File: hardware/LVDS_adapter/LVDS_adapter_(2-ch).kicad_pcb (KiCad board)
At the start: 2 copper layers, 26 x 25.8 mm, 10 parts, among them J1 DF12NB(3.0)-30DS-0.5V(51), J2 LVDS, J3 BL_POWER, J4 DF12NB(3.0)-30DS-0.5V(51)

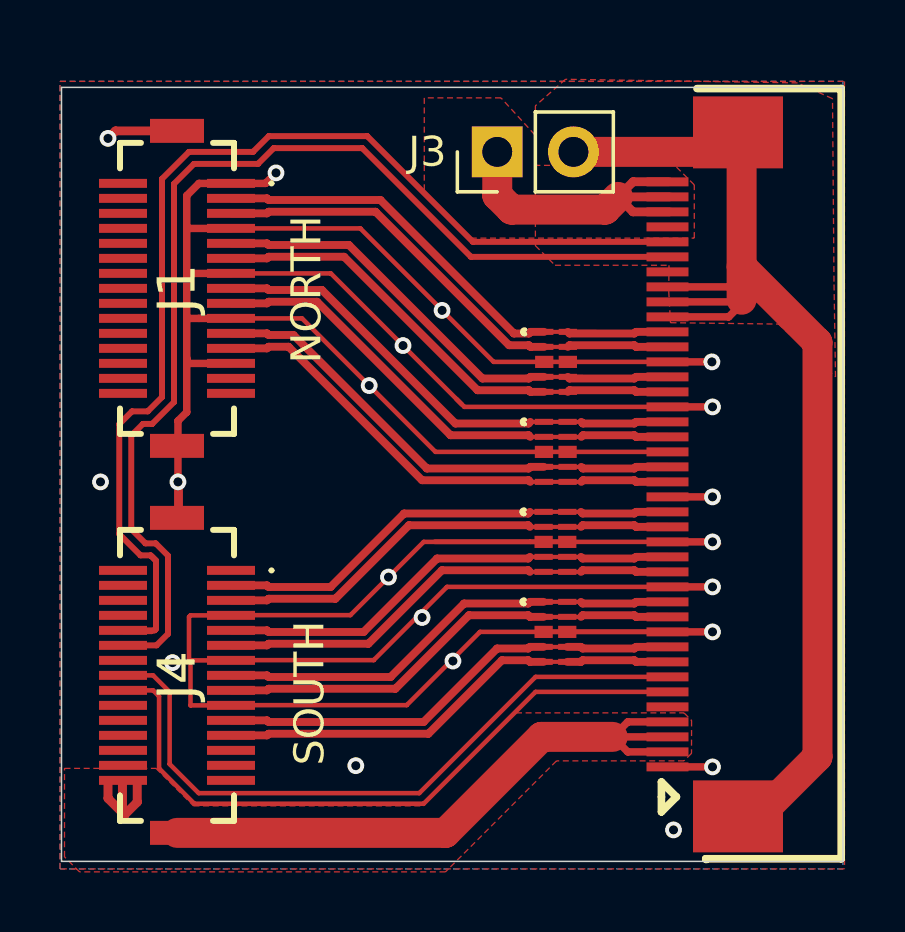
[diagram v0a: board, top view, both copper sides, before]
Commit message: make 4 layers for better signal integrity and add DC-DC for backlight
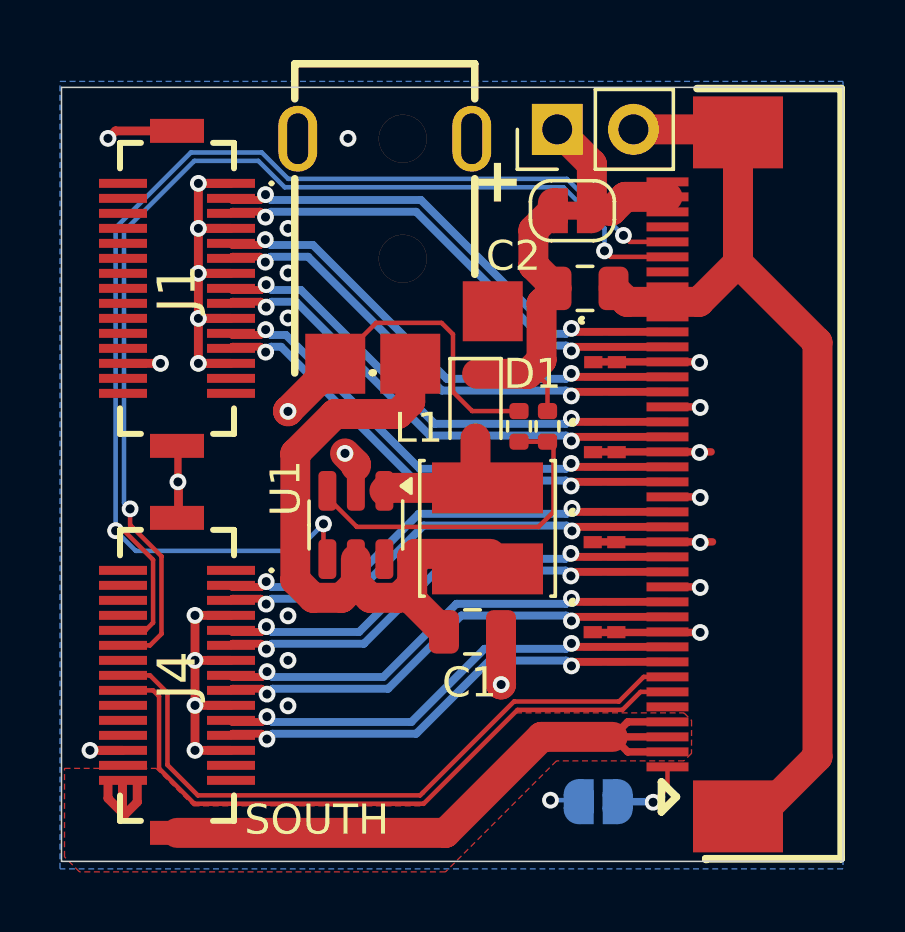
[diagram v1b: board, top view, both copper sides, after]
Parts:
- added C1: 10uF 25V, Capacitor_SMD:C_0805_2012Metric, F.Cu at (138.5, 94.6)
- added C2: 10uF 25V, Capacitor_SMD:C_0805_2012Metric, F.Cu at (142.2, 83.2)
- added D1: 1N5819WS, Diode_SMD:D_SOD-323, F.Cu at (138.6, 87.1)
- added J5: Barrel_Jack_MountingPin, easyeda2kicad:DC-IN-SMD_DC-045A-13A, F.Cu at (135.9, 81.9)
- added JP1: SolderJumper_2_Open, Jumper:SolderJumper-2_P1.3mm_Open_RoundedPad1.0x1.5mm, B.Cu at (142.7, 100.3)
- added JP3: SolderJumper_2_Bridged, Jumper:SolderJumper-2_P1.3mm_Bridged_RoundedPad1.0x1.5mm, F.Cu at (141.8, 80.6)
- added L1: 22uH, Inductor_SMD:L_Cenker_CKCS4020, F.Cu at (139.0, 91.2)
- added R2: 8.06K 1%, Resistor_SMD:R_0402_1005Metric, F.Cu at (140.1, 87.8)
- added R3: 150K 1%, Resistor_SMD:R_0402_1005Metric, F.Cu at (141.0, 87.8)
- added U1: MT3608, Package_TO_SOT_SMD:SOT-23-6, F.Cu at (134.6, 91.0)
- moved G*** 21.3 mm to (128.3, 78.3), turned to 0 degrees
- moved G*** 16.1 mm to (128.7, 92.7), turned to 90 degrees
- moved J3 2.14 mm to (141.3, 77.8)
- moved CR1 1.64 mm to (142.9, 85.6)
- moved CR2 1.64 mm to (142.9, 88.6)
- moved CR3 1.64 mm to (142.9, 91.6)
- moved CR4 1.64 mm to (142.9, 94.6)
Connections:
- CR1 pad 1: LVDS_OC_P -> LVDS_EC_P
- CR1 pad 10: LVDS_OC_P -> LVDS_EC_P
- CR1 pad 2: LVDS_OC_N -> LVDS_EC_N
- CR1 pad 4: LVDS_O2_P -> LVDS_E2_P
- CR1 pad 5: LVDS_O2_N -> LVDS_E2_N
- CR1 pad 6: LVDS_O2_N -> LVDS_E2_N
- CR1 pad 7: LVDS_O2_P -> LVDS_E2_P
- CR1 pad 9: LVDS_OC_N -> LVDS_EC_N
- CR2 pad 1: LVDS_O1_P -> LVDS_E1_P
- CR2 pad 10: LVDS_O1_P -> LVDS_E1_P
- CR2 pad 2: LVDS_O1_N -> LVDS_E1_N
- CR2 pad 4: LVDS_O0_P -> LVDS_E0_P
- CR2 pad 5: LVDS_O0_N -> LVDS_E0_N
- CR2 pad 6: LVDS_O0_N -> LVDS_E0_N
- CR2 pad 7: LVDS_O0_P -> LVDS_E0_P
- CR2 pad 9: LVDS_O1_N -> LVDS_E1_N
- CR3 pad 1: LVDS_EC_P -> LVDS_OC_P
- CR3 pad 10: LVDS_EC_P -> LVDS_OC_P
- CR3 pad 2: LVDS_EC_N -> LVDS_OC_N
- CR3 pad 4: LVDS_E2_P -> LVDS_O2_P
- CR3 pad 5: LVDS_E2_N -> LVDS_O2_N
- CR3 pad 6: LVDS_E2_N -> LVDS_O2_N
- CR3 pad 7: LVDS_E2_P -> LVDS_O2_P
- CR3 pad 9: LVDS_EC_N -> LVDS_OC_N
- CR4 pad 1: LVDS_E1_P -> LVDS_O1_P
- CR4 pad 10: LVDS_E1_P -> LVDS_O1_P
- CR4 pad 2: LVDS_E1_N -> LVDS_O1_N
- CR4 pad 4: LVDS_E0_P -> LVDS_O0_P
- CR4 pad 5: LVDS_E0_N -> LVDS_O0_N
- CR4 pad 6: LVDS_E0_N -> LVDS_O0_N
- CR4 pad 7: LVDS_E0_P -> LVDS_O0_P
- CR4 pad 9: LVDS_E1_N -> LVDS_O1_N
- J1 pad 11: LVDS_O2_N -> LVDS_E2_N
- J1 pad 15: LVDS_O1_P -> LVDS_E1_P
- J1 pad 17: LVDS_O1_N -> LVDS_E1_N
- J1 pad 21: LVDS_O0_P -> LVDS_E0_P
- J1 pad 23: LVDS_O0_N -> LVDS_E0_N
- J1 pad 3: LVDS_OC_P -> LVDS_EC_P
- J1 pad 5: LVDS_OC_N -> LVDS_EC_N
- J1 pad 9: LVDS_O2_P -> LVDS_E2_P
- J2 pad 1: GND -> Net-(J2-Pin_1)
- J2 pad 11: LVDS_E1_N -> LVDS_O1_N
- J2 pad 12: LVDS_E1_P -> LVDS_O1_P
- J2 pad 14: LVDS_E2_N -> LVDS_O2_N
- J2 pad 15: LVDS_E2_P -> LVDS_O2_P
- J2 pad 17: LVDS_EC_N -> LVDS_OC_N
- J2 pad 18: LVDS_EC_P -> LVDS_OC_P
- J2 pad 20: LVDS_O0_N -> LVDS_E0_N
- J2 pad 21: LVDS_O0_P -> LVDS_E0_P
- J2 pad 23: LVDS_O1_N -> LVDS_E1_N
- J2 pad 24: LVDS_O1_P -> LVDS_E1_P
- J2 pad 26: LVDS_O2_N -> LVDS_E2_N
- J2 pad 27: LVDS_O2_P -> LVDS_E2_P
- J2 pad 29: LVDS_OC_N -> LVDS_EC_N
- J2 pad 30: LVDS_OC_P -> LVDS_EC_P
- J2 pad 6: SDA2 -> SCL2
- J2 pad 7: SCL2 -> SDA2
- J2 pad 8: LVDS_E0_N -> LVDS_O0_N
- J2 pad 9: LVDS_E0_P -> LVDS_O0_P
- J4 pad 11: LVDS_E2_N -> LVDS_O2_N
- J4 pad 15: LVDS_E1_P -> LVDS_O1_P
- J4 pad 16: SCL2 -> SDA2
- J4 pad 17: LVDS_E1_N -> LVDS_O1_N
- J4 pad 18: SDA2 -> SCL2
- J4 pad 21: LVDS_E0_P -> LVDS_O0_P
- J4 pad 23: LVDS_E0_N -> LVDS_O0_N
- J4 pad 24: unconnected-(J4-23-Pad24) -> Net-(J4-23)
- J4 pad 3: LVDS_EC_P -> LVDS_OC_P
- J4 pad 5: LVDS_EC_N -> LVDS_OC_N
- J4 pad 9: LVDS_E2_P -> LVDS_O2_P
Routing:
- net GND: track 146.1 -> 47.4 mm, vias 20 -> 28
- net +5V: track 0.00 -> 21.1 mm
- net Net-(U1-FB): track 0.00 -> 11.7 mm
- net Net-(D1-K): track 0.00 -> 11.5 mm
- net LED_GND: track 39.5 -> 46.7 mm, vias 0 -> 3
- net /BL_EN: track 38.0 -> 44.7 mm, vias 0 -> 3
- net LED_VCC: track 11.4 -> 5.90 mm
- net Net-(D1-A): track 0.00 -> 5.29 mm
- net Net-(J2-Pin_1): track 0.00 -> 2.57 mm, vias 0 -> 1
- net LVDS_O2_P: track 17.7 -> 15.9 mm, vias 0 -> 2
- net LVDS_O2_N: track 17.6 -> 15.9 mm, vias 0 -> 2
- net LVDS_OC_N: track 17.5 -> 15.9 mm, vias 0 -> 2
- net LVDS_OC_P: track 17.4 -> 15.9 mm, vias 0 -> 2
- net LVDS_O0_P: track 17.1 -> 15.9 mm, vias 0 -> 2
- net LVDS_EC_N: track 15.7 -> 16.7 mm, vias 0 -> 2
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- added copper zone on In2.Cu, net GND
- added copper zone on In1.Cu, net LED_GND
- removed copper zone on F.Cu, net GND
- removed copper zone on F.Cu, net LED_GND
- removed copper zone on F.Cu, net LED_VCC
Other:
- copper layers 2 -> 4
- board text added: "+"
- board text added: "LVDS adapter v0.11"
- board text added: "VERSION:"
- board text removed: "LVDS adapter board"
- board text removed: "NORTH"
- board text removed: "NOTE: copper fill was corrected (too many short circuits on FPC connector)"

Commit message: review and update manufacturing constraints (via size, etc.)
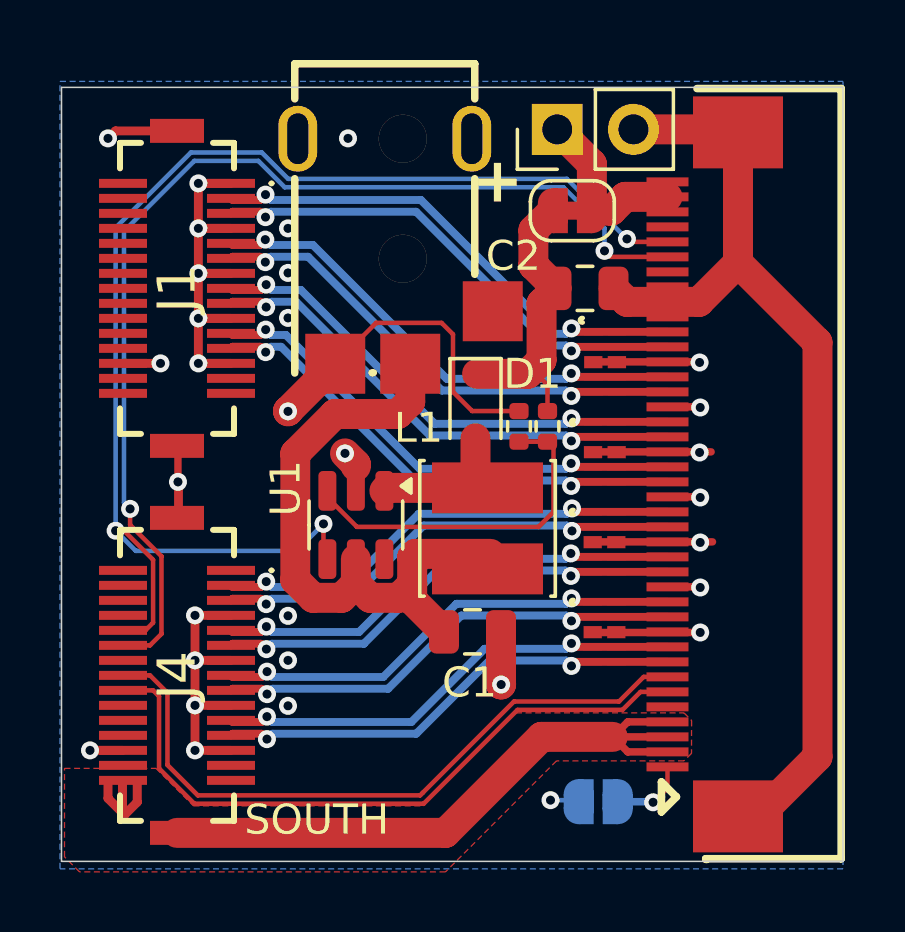
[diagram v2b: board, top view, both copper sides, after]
